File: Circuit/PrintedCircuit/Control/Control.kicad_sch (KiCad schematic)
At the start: 10 parts, among them J1 Conn_01x07_Pin, J2 Conn_01x07_Pin, J3 Conn_01x07_Pin, J4 Conn_01x07_Pin, J5 Conn_01x07_Pin, J6 Conn_01x07_Pin, J7 Conn_01x07_Pin, J8 Conn_01x07_Pin, J9 Conn_01x02_Pin, U1 Pico

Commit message: Control基板完成
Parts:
- removed J9: Conn_01x02_Pin, Connector_JST:JST_XH_B2B-XH-A_1x02_P2.50mm_Vertical, symbol Connector:Conn_01x02_Pin
- added J9: Conn_01x06_Pin, Connector_JST:JST_XH_B6B-XH-A_1x06_P2.50mm_Vertical, symbol Connector:Conn_01x06_Pin
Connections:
- net +3.3V: now also J9.1 (Pin_1)
- net GND: now also U1.42 (GND), J9.2 (Pin_2)
- net UART_RX: now also J9.5 (Pin_5)
- net UART_TX: now also J9.6 (Pin_6)
- net SWCLK: now reaches U1.41 (SWCLK)
- net SWCLK: now also J9.4 (Pin_4)
- net SWDIO: now reaches U1.43 (SWDIO)
- net SWDIO: now also J9.3 (Pin_3)

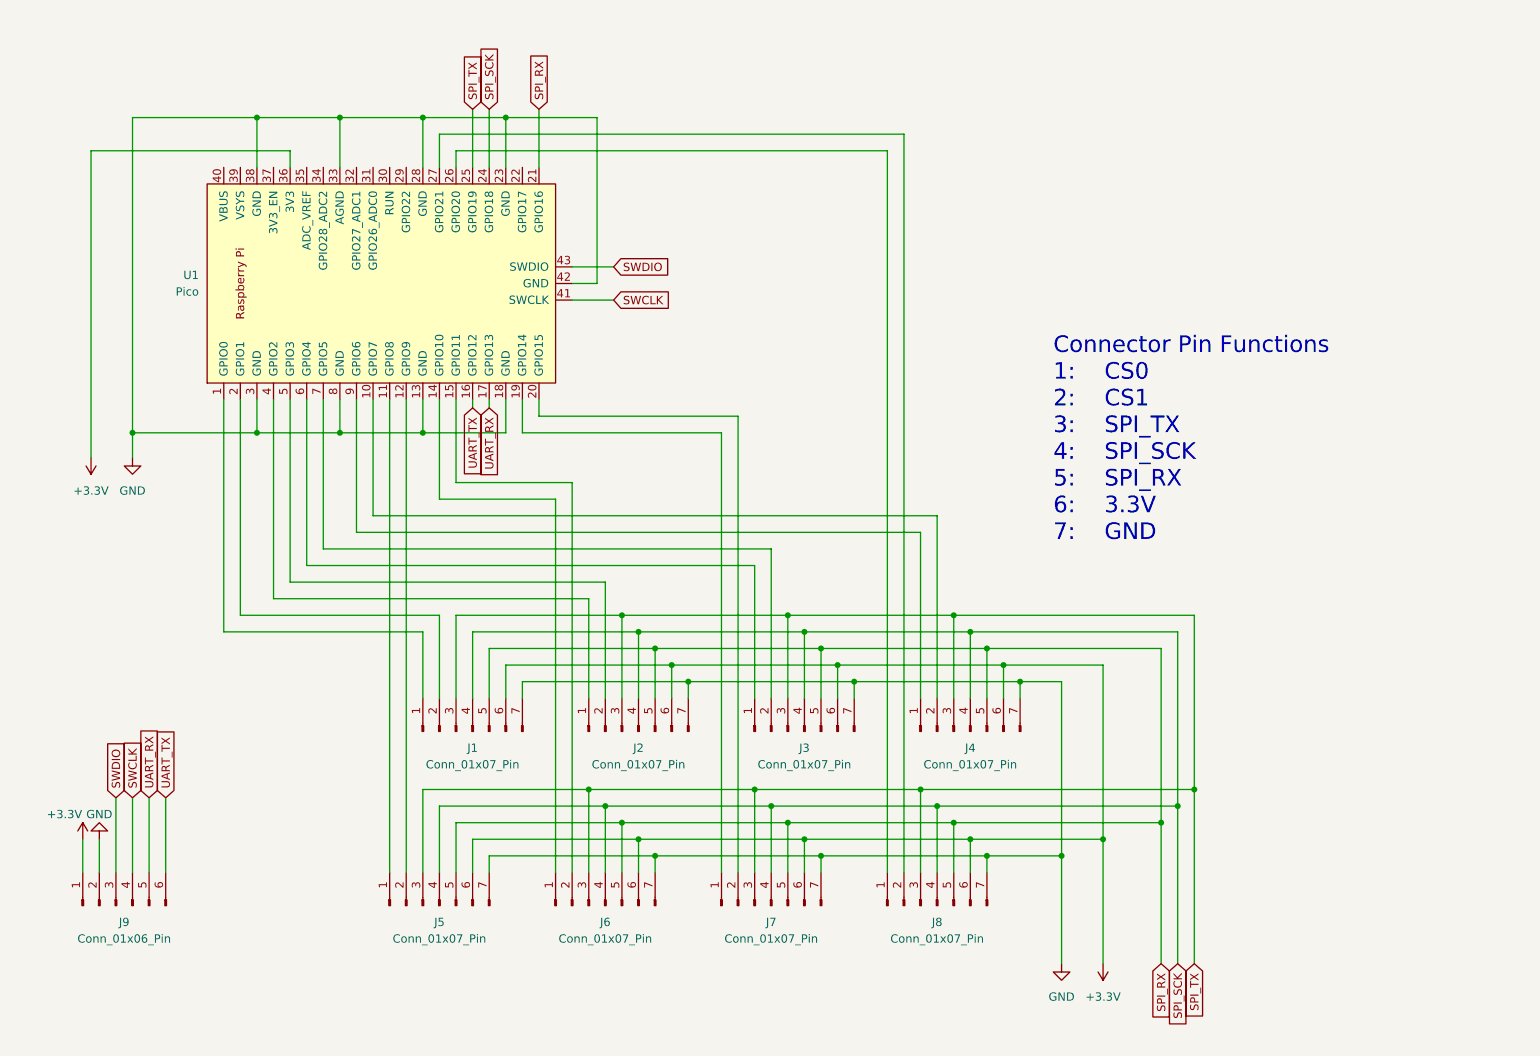
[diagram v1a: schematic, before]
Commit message: 基盤にテストポイントを追加、SMUにDACとPSを追加
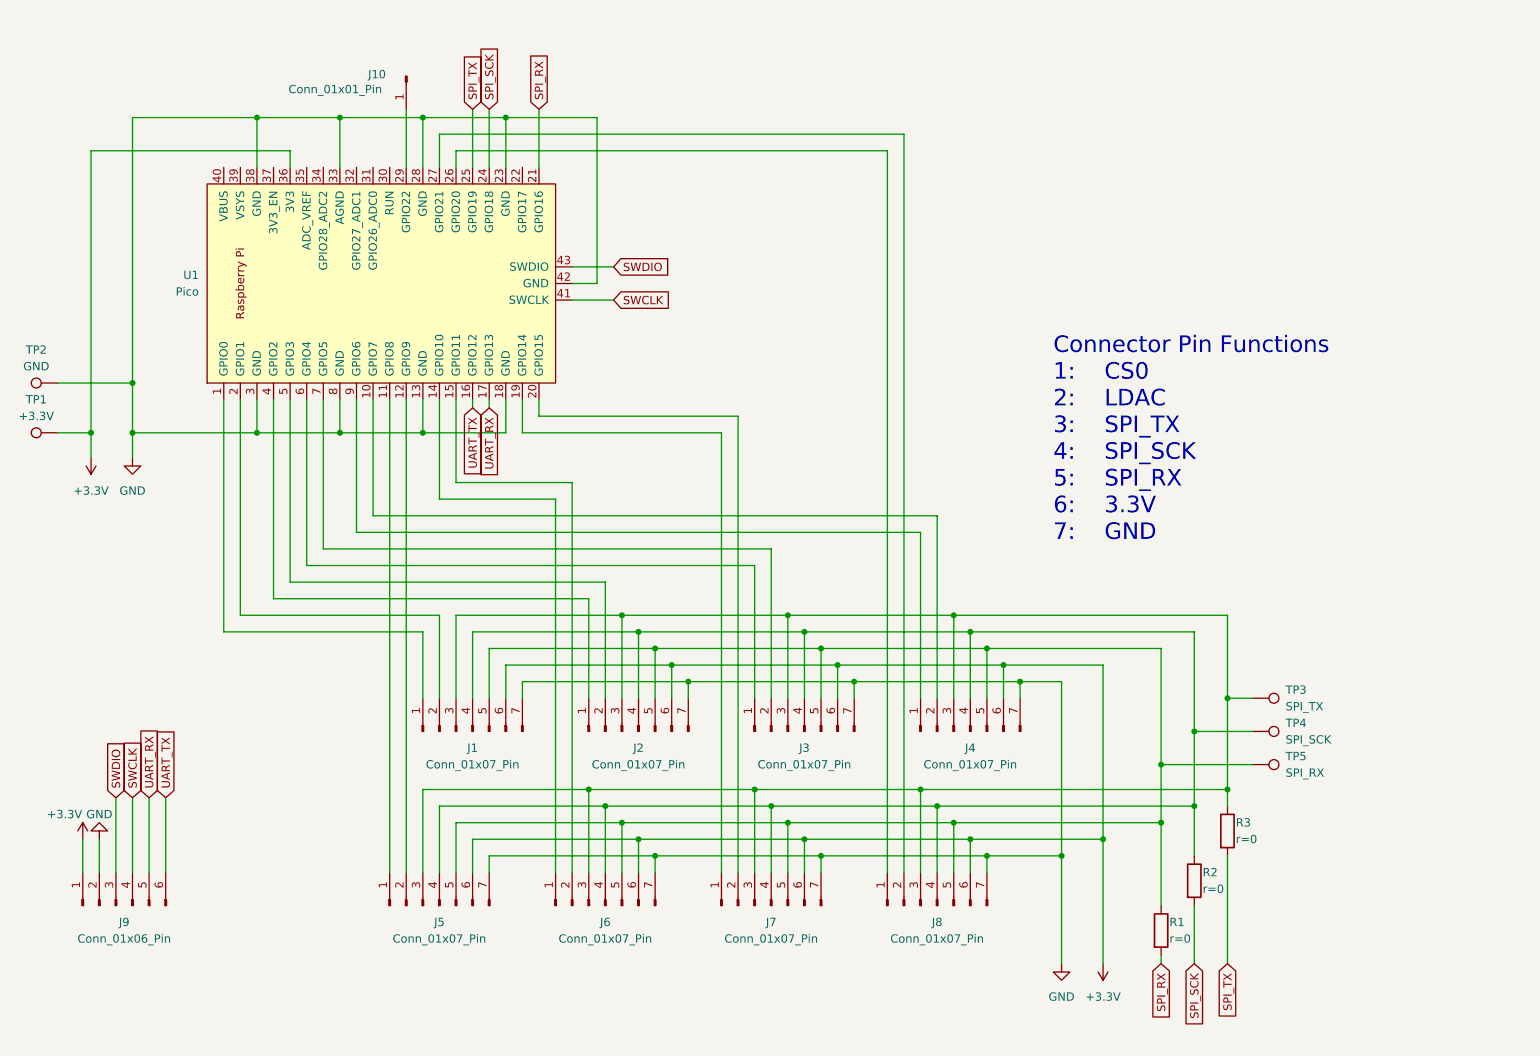
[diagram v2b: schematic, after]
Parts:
- added J10: Conn_01x01_Pin, symbol Connector:Conn_01x01_Pin
- added R1, R2, R3: ${SIM.PARAMS}, Resistor_SMD:R_0603_1608Metric_Pad0.98x0.95mm_HandSolder, symbol Device:R
- added TP1: +3.3V, symbol Connector:TestPoint
- added TP2: GND, symbol Connector:TestPoint
- added TP3: SPI_TX, symbol Connector:TestPoint
- added TP4: SPI_SCK, symbol Connector:TestPoint
- added TP5: SPI_RX, symbol Connector:TestPoint
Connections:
- net +3.3V: now also TP1.1
- net GND: now also TP2.1
- net SPI_RX: now also R1.2; no longer J1.5 (Pin_5), J2.5 (Pin_5), J3.5 (Pin_5), J4.5 (Pin_5), J5.5 (Pin_5), J6.5 (Pin_5), J7.5 (Pin_5), J8.5 (Pin_5)
- net SPI_SCK: now also R2.2; no longer J1.4 (Pin_4), J2.4 (Pin_4), J3.4 (Pin_4), J4.4 (Pin_4), J5.4 (Pin_4), J6.4 (Pin_4), J7.4 (Pin_4), J8.4 (Pin_4)
- net SPI_TX: now also R3.2; no longer J1.3 (Pin_3), J2.3 (Pin_3), J3.3 (Pin_3), J4.3 (Pin_3), J5.3 (Pin_3), J6.3 (Pin_3), J7.3 (Pin_3), J8.3 (Pin_3)
- net at U1.29 (GPIO22): now also J10.1 (Pin_1)
- new net: J1.3 (Pin_3), J2.3 (Pin_3), J3.3 (Pin_3), J4.3 (Pin_3), J5.3 (Pin_3), J6.3 (Pin_3), J7.3 (Pin_3), J8.3 (Pin_3), R3.1, TP3.1
- new net: J1.4 (Pin_4), J2.4 (Pin_4), J3.4 (Pin_4), J4.4 (Pin_4), J5.4 (Pin_4), J6.4 (Pin_4), J7.4 (Pin_4), J8.4 (Pin_4), R2.1, TP4.1
- new net: J1.5 (Pin_5), J2.5 (Pin_5), J3.5 (Pin_5), J4.5 (Pin_5), J5.5 (Pin_5), J6.5 (Pin_5), J7.5 (Pin_5), J8.5 (Pin_5), R1.1, TP5.1
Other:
- note added: "Connector Pin Functions 1: CS0 2: LDAC 3: SPI_TX 4: SPI_SCK 5: SPI_RX 6: 3.3V 7: GND"
- note removed: "Connector Pin Functions 1: CS0 2: CS1 3: SPI_TX 4: SPI_SCK 5: SPI_RX 6: 3.3V 7: GND"

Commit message: 保護回路のシミュレーションを追加
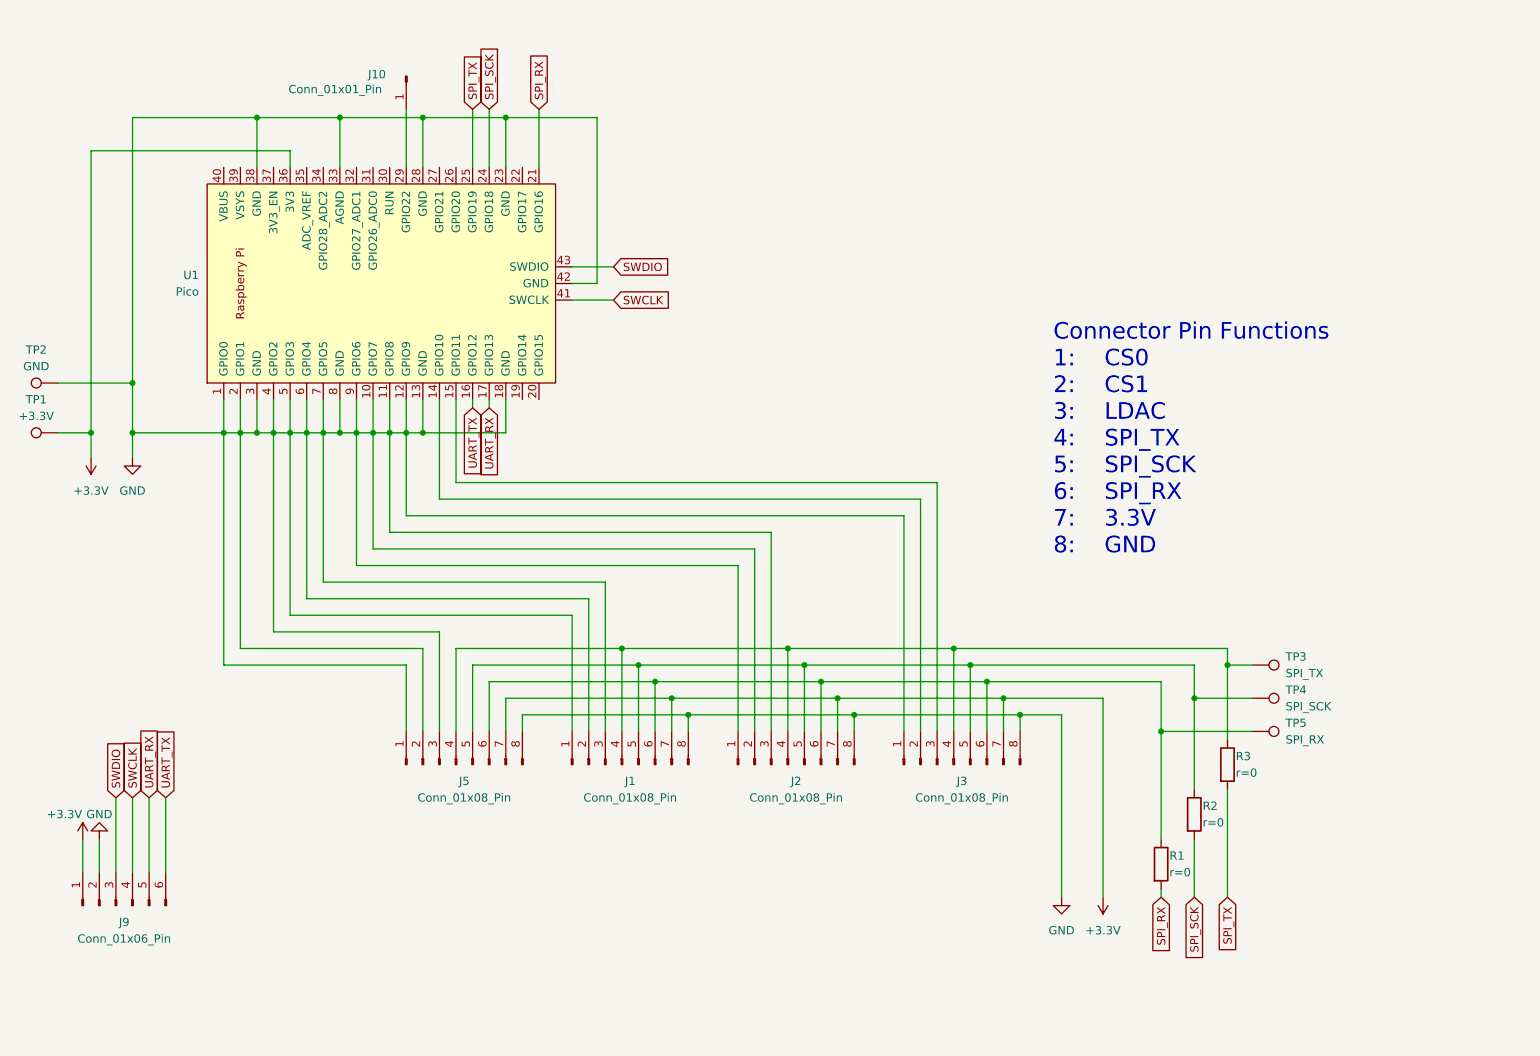
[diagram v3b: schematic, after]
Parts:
- removed J1, J2, J3, J4, J5, J6, J7, J8: Conn_01x07_Pin, Connector_JST:JST_XH_B7B-XH-A_1x07_P2.50mm_Vertical, symbol Connector:Conn_01x07_Pin
- added J1, J2, J3, J5: Conn_01x08_Pin, symbol Connector:Conn_01x08_Pin
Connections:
- net +3.3V: now also J1.7 (Pin_7), J2.7 (Pin_7), J3.7 (Pin_7), J5.7 (Pin_7)
- net GND: now also U1.1 (GPIO0), U1.10 (GPIO7), U1.11 (GPIO8), U1.12 (GPIO9), U1.2 (GPIO1), U1.4 (GPIO2), U1.5 (GPIO3), U1.6 (GPIO4), U1.7 (GPIO5), U1.9 (GPIO6), J1.1 (Pin_1), J1.2 (Pin_2), J1.3 (Pin_3), J1.8 (Pin_8), J2.1 (Pin_1), J2.2 (Pin_2), J2.3 (Pin_3), J2.8 (Pin_8), J3.1 (Pin_1), J3.8 (Pin_8), J5.1 (Pin_1), J5.2 (Pin_2), J5.3 (Pin_3), J5.8 (Pin_8)
- net at R3.1, TP3.1: now also J1.4 (Pin_4), J2.4 (Pin_4), J3.4 (Pin_4), J5.4 (Pin_4)
- net at R2.1, TP4.1: now also J1.5 (Pin_5), J2.5 (Pin_5), J3.5 (Pin_5), J5.5 (Pin_5)
- net at R1.1, TP5.1: now also J1.6 (Pin_6), J2.6 (Pin_6), J3.6 (Pin_6), J5.6 (Pin_6)
- net at U1.14 (GPIO10): now also J3.2 (Pin_2)
- net at U1.15 (GPIO11): now also J3.3 (Pin_3)
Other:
- note added: "Connector Pin Functions 1: CS0 2: CS1 3: LDAC 4: SPI_TX 5: SPI_SCK 6: SPI_RX 7: 3.3V 8: GND"
- note removed: "Connector Pin Functions 1: CS0 2: LDAC 3: SPI_TX 4: SPI_SCK 5: SPI_RX 6: 3.3V 7: GND"
- moved on the sheet: R1, R2, R3, TP3, TP4, TP5

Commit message: フットプリント設定
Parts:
- removed J10: Conn_01x01_Pin, symbol Connector:Conn_01x01_Pin
- removed TP1: +3.3V, symbol Connector:TestPoint
- removed TP2: GND, symbol Connector:TestPoint
- removed TP3: SPI_TX, symbol Connector:TestPoint
- removed TP4: SPI_SCK, symbol Connector:TestPoint
- removed TP5: SPI_RX, symbol Connector:TestPoint
- added J1: Conn_01x06_Pin, Connector_PinHeader_2.54mm:PinHeader_1x06_P2.54mm_Vertical, symbol Connector:Conn_01x06_Pin
- J2: renamed from J5; footprint (none) -> Connector_JST:JST_XH_B8B-XH-A_1x08_P2.50mm_Vertical
- J3: renamed from J1; footprint (none) -> Connector_JST:JST_XH_B8B-XH-A_1x08_P2.50mm_Vertical
- J4: renamed from J2; footprint (none) -> Connector_JST:JST_XH_B8B-XH-A_1x08_P2.50mm_Vertical
- J5: renamed from J3; footprint (none) -> Connector_JST:JST_XH_B8B-XH-A_1x08_P2.50mm_Vertical
- renumbered J9 to J6, R3 to R1, R1 to R3
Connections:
- net +3.3V: now also J1.5 (Pin_5)
- net GND: now also J1.6 (Pin_6)
- net at J2.4 (Pin_4), J3.4 (Pin_4), J4.4 (Pin_4)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: now also J1.1 (Pin_1)
- net at J2.5 (Pin_5), J3.5 (Pin_5), J4.5 (Pin_5)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: now also J1.2 (Pin_2)
- net at J2.6 (Pin_6), J3.6 (Pin_6), J4.6 (Pin_6)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: now also J1.3 (Pin_3)
- net TEST_GPIO: now reaches U1.29 (GPIO22)
- net TEST_GPIO: now also J1.4 (Pin_4)
